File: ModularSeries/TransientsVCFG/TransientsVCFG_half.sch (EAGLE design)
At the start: 151 parts, among them IC2 4013N, IC6 4013N, Q1 2N3906, Q10 2N3906, Q11 2N3904, Q12 2N3904, Q2 2N3906, Q3 2N3906, Q4 2N3906, Q5 2N3904, Q6 2N3904, Q7 2N3906, Q8 2N3906, Q9 2N3906

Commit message: Folder cleaned up, Transients added
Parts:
- removed BOTH2, DN_CV2, DPOT2, INPUT2, OUT2, UPOT2, UP_CV2: 1XWIREPAD, ElectricNoodleBox:1XWIREPAD
- removed C11, C14, C15, C16, C17, C18, C19, C20: 100nF, rcl:C-EU050-025X075
- removed C12, C13: 100pF, rcl:C-EU050-025X075
- removed D10, D11, D12, D13, D14, D8, D9: BAT85, ElectricNoodleBox:SCHOTTKY_DO35
- removed IC5: (no value), ElectricNoodleBox:LM13700DIL
- removed IC6: 4013N, 40xx:4013N
- removed IC7: (no value), ElectricNoodleBox:TL0X4DIL
- removed IC8: (no value), ElectricNoodleBox:TL0X2DIL
- removed LOOP2, SEL2: 2XWIREPAD, ElectricNoodleBox:2XWIREPAD
- removed Q10, Q7, Q8, Q9: 2N3906, transistor-pnp:2N3906
- removed Q11, Q12: 2N3904, transistor-npn:2N3904
- removed R26, R33, R58: 10K, rcl:R-EU_0207/10
- removed R31, R42: 2K, rcl:R-EU_0207/10
- removed R32: 10K, rcl:R-TRIMM3296W
- removed R34: 100Ω, rcl:R-EU_0207/10
- removed R35, R36, R41, R43, R44, R49, R50, R51, R52, R53: 100K, rcl:R-EU_0207/10
- removed R37, R45: 100Ω, rcl:R-TRIMM3296W
- removed R38, R46: 75Ω, rcl:R-EU_0207/10
- removed R39, R47: 22K, rcl:R-EU_0207/10
- removed R40, R48: 1M, rcl:R-EU_0207/10
- removed R54, R55: 15K, rcl:R-EU_0207/10
- removed R56: 470Ω, rcl:R-EU_0207/10
- removed R57: 150K, rcl:R-EU_0207/10
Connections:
- removed net BOTH_CV2: BOTH2.1, R41.1, R49.1
- removed net IABC_N2: IC5B1.AMPBIAS, Q10.C
- removed net IABC_P2: IC5A1.AMPBIAS, Q8.C
- removed net N$16: IC5A1.AMP+, IC5B1.AMP+, R26.2, R32.E
- removed net N$17: C11.1, D8.C, D9.A, IC8B.+IN
- removed net N$35: IC8A.+IN, IC8B.-IN, IC8B.OUT, R33.2, R51.2, R54.2
- removed net N$43: D8.A, IC5A1.AMPOUT
- removed net N$44: D9.C, IC5B1.AMPOUT
- removed net N$45: IC5A1.AMP-, IC5B1.AMP-, R32.A, R33.1
- removed net N$46: IC8A.-IN, IC8A.OUT, R34.1
- removed net N$47: IC7C.-IN, R31.1, R35.2, R36.2, R41.2
- removed net N$48: IC7C.OUT, R31.2, R37.E
- removed net N$49: R37.A, R38.2
- removed net N$50: Q7.B, R37.S
- removed net N$51: Q7.E, Q8.E, R39.1
- removed net N$52: C12.1, D10.A, IC7D.OUT
- removed net N$53: C12.2, IC7D.-IN, Q7.C, R40.1
- removed net N$54: R36.1, UP_CV2.1
- removed net N$55: R35.1, UPOT2.1
- removed net N$56: OUT2.1, R34.2
- removed net N$57: IC7B.-IN, R42.1, R43.2, R44.2, R49.2
- removed net N$58: IC7B.OUT, R42.2, R45.E
- removed net N$59: R45.A, R46.2
- removed net N$60: Q9.B, R45.S
- removed net N$61: Q10.E, Q9.E, R47.1
- removed net N$62: C13.1, D11.A, IC7A.OUT
- removed net N$63: C13.2, IC7A.-IN, Q9.C, R48.1
- removed net N$64: DN_CV2.1, R44.1
- removed net N$65: DPOT2.1, R43.1
- removed net N$66: IC6A.R, IC6B.!Q, IC6B.D, R53.1
- removed net N$67: IC5A2.BUFF_OUT, IC6A.S, LOOP2.2, R50.1
- removed net N$68: R26.1, SEL2.2
- removed net N$69: IC6A.Q, SEL2.1
- removed net N$70: D13.C, IC6B.CLK, R51.1, R52.1
- removed net N$72: D11.C, R47.2
- removed net N$73: D10.C, R39.2
- removed net N$74: Q11.C, Q12.B, R55.2, R57.1
- removed net N$75: LOOP2.1, Q12.E, R56.2
- removed net N$76: D14.C, Q11.B, R54.1, R57.2
- removed net N$77: INPUT2.1, R58.1
- removed net N$78: D12.C, IC5A2.BUFF_IN, R58.2
- net +12V: no longer C14.1, C16.1, C18.1, C20.1, IC5P.V+, IC6P.VDD, IC7P.V+, IC8P.V+, Q12.C, R55.1
- net -10VREF: no longer R40.2, R48.2
- net -12V: no longer C15.2, C17.2, C19.2, IC5P.V-, IC7P.V-, IC8P.V-
- net AGND: no longer C11.2, C14.2, C15.1, C16.2, C17.1, C18.2, C19.1, C20.2, D12.A, D13.A, D14.A, IC6A.CLK, IC6A.D, IC6B.R, IC6B.S, IC6P.VSS, IC7A.+IN, IC7B.+IN, IC7C.+IN, IC7D.+IN, Q10.B, Q11.E, Q8.B, R32.S, R38.1, R46.1, R50.2, R52.2, R53.2, R56.1
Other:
- note added: "Transients Voltage Controlled Function Generator (1 half) Electric Noodle Box Aidan Taylor 2020"
- note removed: "Film Type e.g PET for C11"
- moved on the sheet: +10VR1, +10VR2, +12V1, +12V2, -10VR1, -10VR2, BOTH1, C10, C2, C21, C22, C3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

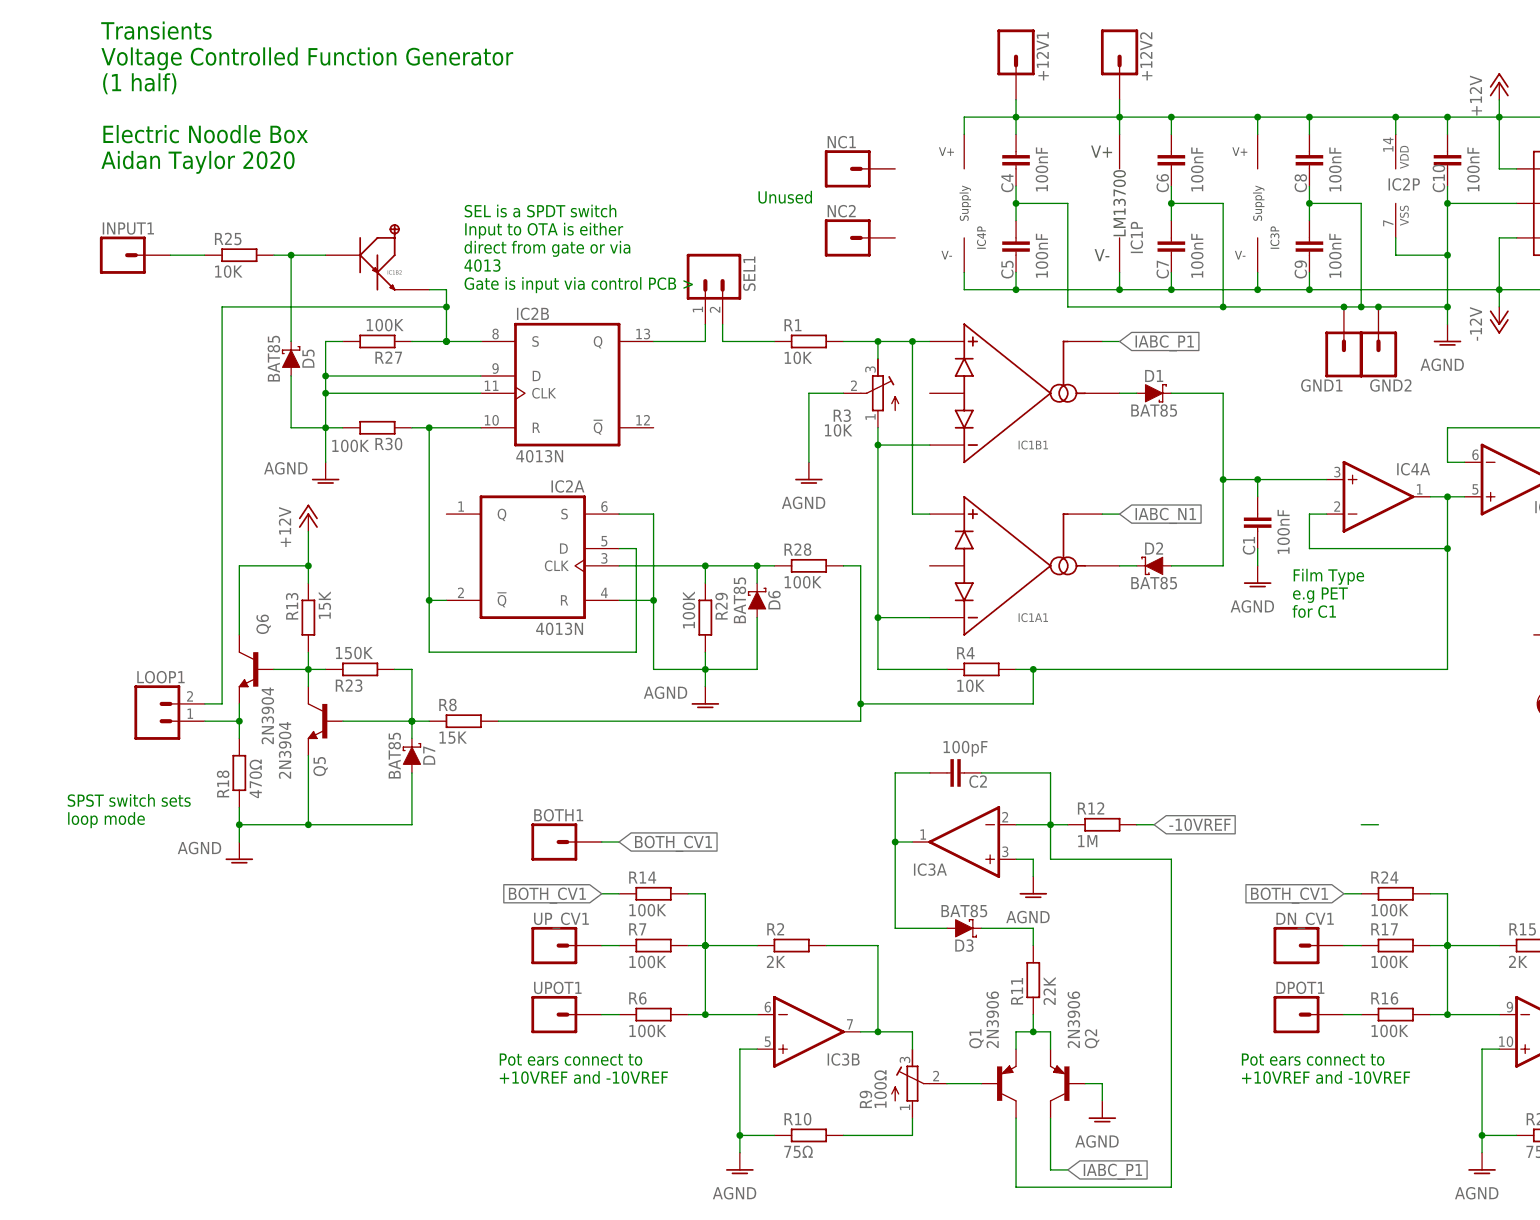
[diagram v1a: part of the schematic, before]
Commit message: Updates to Transients core including images and BOM
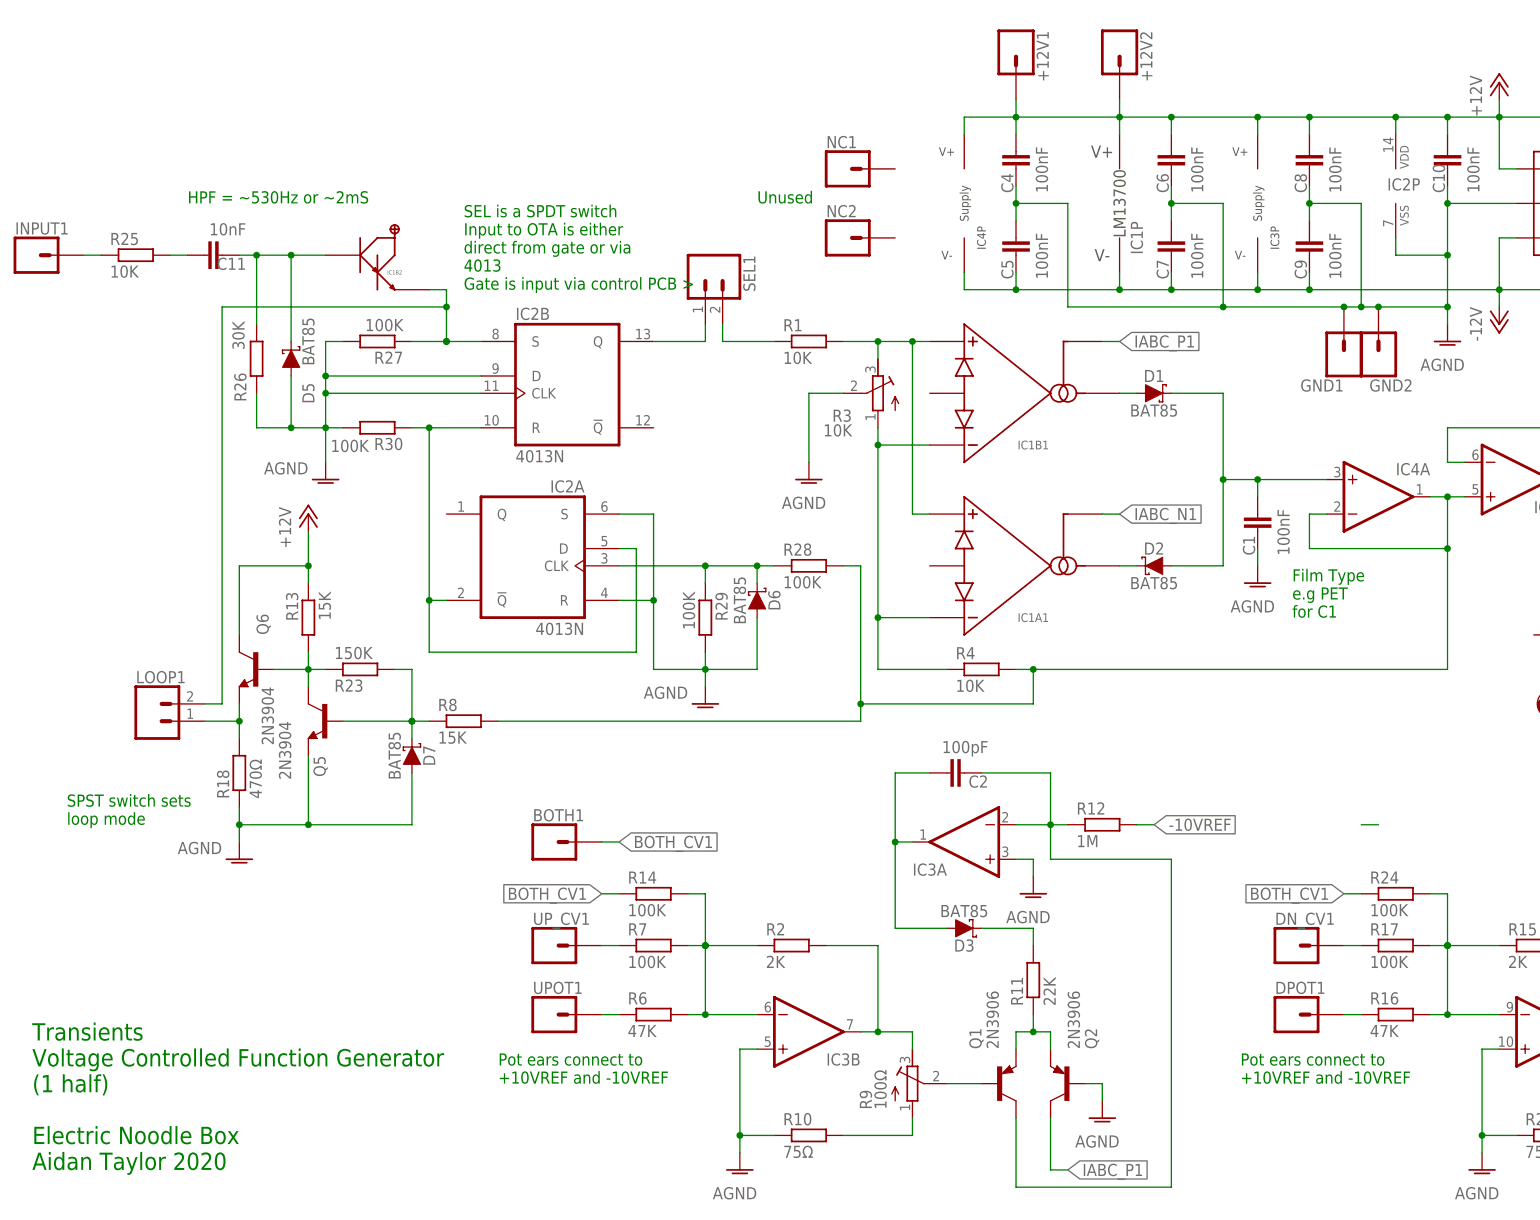
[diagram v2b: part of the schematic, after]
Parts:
- added C11: 10nF, rcl:C-EU050-025X075
- added R26: 30K, rcl:R-EU_0207/10
- R16, R6: value 100K -> 47K
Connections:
- removed net N$40: D5.C, IC1B2.BUFF_IN, R25.2
- new net N$16: C11.1, R25.2
- new net N$17: C11.2, D5.C, IC1B2.BUFF_IN, R26.2
- net AGND: now also R26.1
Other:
- note added: "HPF = ~530Hz or ~2mS"
- moved on the sheet: INPUT1, R25
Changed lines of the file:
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@@
 <part name="IC4" library="ElectricNoodleBox" deviceset="TL0X2" device="DIL" package3d_urn="urn:adsk.eagle:package:29519/2"/>
 <part name="AGND3" library="supply1" library_urn="urn:adsk.eagle:library:371" deviceset="AGND" device=""/>
-<part name="R6" library="rcl" library_urn="urn:adsk.eagle:library:334" deviceset="R-EU_" device="0207/10" package3d_urn="urn:adsk.eagle:package:23491/2" value="100K"/>
+<part name="R6" library="rcl" library_urn="urn:adsk.eagle:library:334" deviceset="R-EU_" device="0207/10" package3d_urn="urn:adsk.eagle:package:23491/2" value="47K"/>
 <part name="R7" library="rcl" library_urn="urn:adsk.eagle:library:334" deviceset="R-EU_" device="0207/10" package3d_urn="urn:adsk.eagle:package:23491/2" value="100K"/>
 <part name="Q1" library="transistor-pnp" library_urn="urn:adsk.eagle:library:399" deviceset="2N3906" device="" package3d_urn="urn:adsk.eagle:package:29211/2"/>
@@
 <part name="R15" library="rcl" library_urn="urn:adsk.eagle:library:334" deviceset="R-EU_" device="0207/10" package3d_urn="urn:adsk.eagle:package:23491/2" value="2K"/>
 <part name="AGND6" library="supply1" library_urn="urn:adsk.eagle:library:371" deviceset="AGND" device=""/>
-<part name="R16" library="rcl" library_urn="urn:adsk.eagle:library:334" deviceset="R-EU_" device="0207/10" package3d_urn="urn:adsk.eagle:package:23491/2" value="100K"/>
+<part name="R16" library="rcl" library_urn="urn:adsk.eagle:library:334" deviceset="R-EU_" device="0207/10" package3d_urn="urn:adsk.eagle:package:23491/2" value="47K"/>
 <part name="R17" library="rcl" library_urn="urn:adsk.eagle:library:334" deviceset="R-EU_" device="0207/10" package3d_urn="urn:adsk.eagle:package:23491/2" value="100K"/>
 <part name="Q3" library="transistor-pnp" library_urn="urn:adsk.eagle:library:399" deviceset="2N3906" device="" package3d_urn="urn:adsk.eagle:package:29211/2"/>
@@
 <part name="GND2" library="ElectricNoodleBox" deviceset="1XWIREPAD" device=""/>
 <part name="GND1" library="ElectricNoodleBox" deviceset="1XWIREPAD" device=""/>
+<part name="C11" library="rcl" library_urn="urn:adsk.eagle:library:334" deviceset="C-EU" device="050-025X075" package3d_urn="urn:adsk.eagle:package:23637/1" value="10nF"/>
+<part name="R26" library="rcl" library_urn="urn:adsk.eagle:library:334" deviceset="R-EU_" device="0207/10" package3d_urn="urn:adsk.eagle:package:23491/2" value="30K"/>
 </parts>
 <sheets>
@@
 +10VREF and -10VREF</text>
 <text x="0" y="104.14" size="1.778" layer="91">Unused</text>
-<text x="-96.52" y="109.22" size="2.54" layer="91">Transients
+<text x="-106.68" y="-38.1" size="2.54" layer="91">Transients
 Voltage Controlled Function Generator
 (1 half)
 Electric Noodle Box
 Aidan Taylor 2020</text>
+<text x="-83.82" y="104.14" size="1.778" layer="91">HPF = ~530Hz or ~2mS</text>
 </plain>
 <instances>
@@
 <attribute name="VALUE" x="-57.15" y="69.342" size="1.778" layer="96" rot="R180"/>
 </instance>
-<instance part="INPUT1" gate="G$1" x="-93.98" y="96.52" smashed="yes">
-<attribute name="NAME" x="-96.52" y="99.568" size="1.778" layer="95" font="vector"/>
+<instance part="INPUT1" gate="G$1" x="-106.68" y="96.52" smashed="yes">
+<attribute name="NAME" x="-109.22" y="99.568" size="1.778" layer="95" font="vector"/>
 </instance>
 <instance part="D5" gate="G$1" x="-68.58" y="81.28" smashed="yes" rot="MR90">
-<attribute name="NAME" x="-66.04" y="81.28" size="1.778" layer="95" font="vector" rot="MR90" align="center"/>
-<attribute name="VALUE" x="-71.12" y="81.28" size="1.778" layer="96" font="vector" rot="MR90" align="center"/>
+<attribute name="NAME" x="-66.04" y="76.2" size="1.778" layer="95" font="vector" rot="MR90" align="center"/>
+<attribute name="VALUE" x="-66.04" y="83.82" size="1.778" layer="96" font="vector" rot="MR90" align="center"/>
 </instance>
 <instance part="D6" gate="G$1" x="0" y="45.72" smashed="yes" rot="MR90">
@@
 <attribute name="VALUE" x="-62.23" y="38.862" size="1.778" layer="96" rot="MR180"/>
 </instance>
-<instance part="R25" gate="G$1" x="-76.2" y="96.52" smashed="yes">
-<attribute name="NAME" x="-80.01" y="98.0186" size="1.778" layer="95"/>
-<attribute name="VALUE" x="-80.01" y="93.218" size="1.778" layer="96"/>
+<instance part="R25" gate="G$1" x="-91.44" y="96.52" smashed="yes">
+<attribute name="NAME" x="-95.25" y="98.0186" size="1.778" layer="95"/>
+<attribute name="VALUE" x="-95.25" y="93.218" size="1.778" layer="96"/>
 </instance>
 <instance part="H1" gate="G$1" x="116.84" y="30.48" smashed="yes">
@@
 <instance part="GND1" gate="G$1" x="86.36" y="81.28" smashed="yes" rot="R90">
 <attribute name="NAME" x="86.36" y="78.232" size="1.778" layer="95" font="vector" rot="R180"/>
+</instance>
+<instance part="C11" gate="G$1" x="-81.28" y="96.52" smashed="yes" rot="R90">
+<attribute name="NAME" x="-75.184" y="96.139" size="1.778" layer="95" rot="R180"/>
+<attribute name="VALUE" x="-75.184" y="101.219" size="1.778" layer="96" rot="R180"/>
+</instance>
+<instance part="R26" gate="G$1" x="-73.66" y="81.28" smashed="yes" rot="R90">
+<attribute name="NAME" x="-75.1586" y="74.93" size="1.778" layer="95" rot="R90"/>
+<attribute name="VALUE" x="-75.438" y="82.55" size="1.778" layer="96" rot="R90"/>
 </instance>
 </instances>
@@
 <wire x1="-40.64" y1="76.2" x2="-63.5" y2="76.2" width="0.1524" layer="91"/>
 <junction x="-63.5" y="76.2"/>
+<pinref part="R26" gate="G$1" pin="1"/>
+<wire x1="-73.66" y1="76.2" x2="-73.66" y2="71.12" width="0.1524" layer="91"/>
+<wire x1="-73.66" y1="71.12" x2="-68.58" y2="71.12" width="0.1524" layer="91"/>
+<junction x="-68.58" y="71.12"/>
 </segment>
 <segment>
@@
 <pinref part="INPUT1" gate="G$1" pin="1"/>
 <pinref part="R25" gate="G$1" pin="1"/>
-<wire x1="-86.36" y1="96.52" x2="-81.28" y2="96.52" width="0.1524" layer="91"/>
-</segment>
-</net>
-<net name="N$40" class="0">
-<segment>
-<pinref part="R25" gate="G$1" pin="2"/>
-<wire x1="-71.12" y1="96.52" x2="-68.58" y2="96.52" width="0.1524" layer="91"/>
-<pinref part="D5" gate="G$1" pin="C"/>
-<wire x1="-68.58" y1="96.52" x2="-68.58" y2="83.82" width="0.1524" layer="91"/>
-<junction x="-68.58" y="96.52"/>
-<pinref part="IC1" gate="B2" pin="BUFF_IN"/>
-<wire x1="-68.58" y1="96.52" x2="-63.5" y2="96.52" width="0.1524" layer="91"/>
+<wire x1="-99.06" y1="96.52" x2="-96.52" y2="96.52" width="0.1524" layer="91"/>
 </segment>
 </net>
@@
 </segment>
 </net>
+<net name="N$16" class="0">
+<segment>
+<pinref part="R25" gate="G$1" pin="2"/>
+<pinref part="C11" gate="G$1" pin="1"/>
+<wire x1="-86.36" y1="96.52" x2="-83.82" y2="96.52" width="0.1524" layer="91"/>
+</segment>
+</net>
+<net name="N$17" class="0">
+<segment>
+<pinref part="C11" gate="G$1" pin="2"/>
+<wire x1="-76.2" y1="96.52" x2="-73.66" y2="96.52" width="0.1524" layer="91"/>
+<pinref part="R26" gate="G$1" pin="2"/>
+<wire x1="-73.66" y1="96.52" x2="-73.66" y2="86.36" width="0.1524" layer="91"/>
+<pinref part="D5" gate="G$1" pin="C"/>
+<wire x1="-68.58" y1="96.52" x2="-68.58" y2="83.82" width="0.1524" layer="91"/>
+<pinref part="IC1" gate="B2" pin="BUFF_IN"/>
+<wire x1="-68.58" y1="96.52" x2="-63.5" y2="96.52" width="0.1524" layer="91"/>
+<wire x1="-73.66" y1="96.52" x2="-68.58" y2="96.52" width="0.1524" layer="91"/>
+<junction x="-73.66" y="96.52"/>
+<junction x="-68.58" y="96.52"/>
+</segment>
+</net>
